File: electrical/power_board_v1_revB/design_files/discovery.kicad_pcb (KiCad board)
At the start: 2 copper layers, 150 x 100 mm, 18 parts, among them J1 Conn_02x04_CPU, J2 Conn_02x04_PCIe, J3 Conn_02x04_CPU, J4 Conn_02x04_PCIe, J5 Conn_02x04_PCIe, J6 Conn_02x04_PCIe

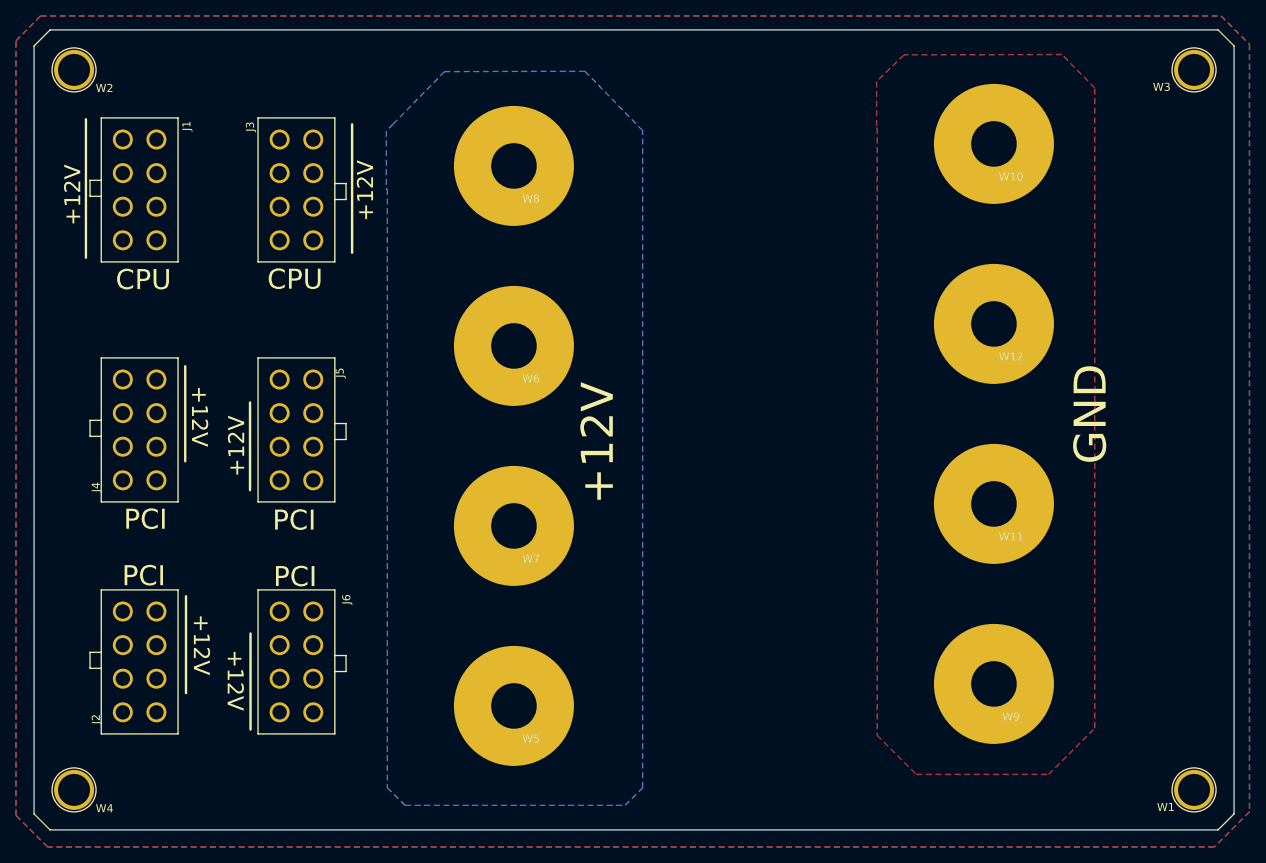
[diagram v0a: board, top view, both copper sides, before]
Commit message: Improvement
PCI connectors on the board have been modified into 2x3pins (2x4 pins originally).
Design and production files have been updated
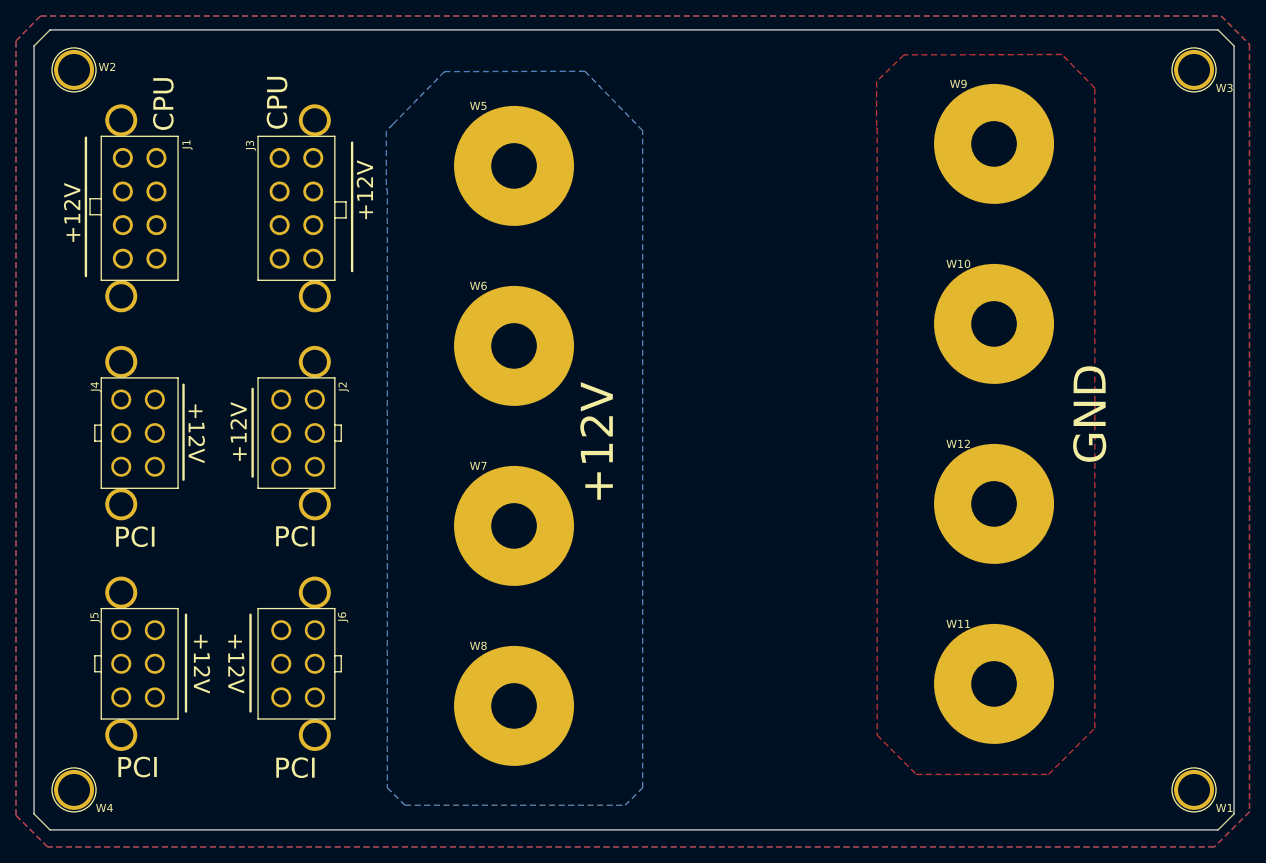
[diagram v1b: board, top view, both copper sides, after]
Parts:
- J1, J3: footprint footprint_cts:CONN_02x04_4.2mm -> discovery:CONN_02x04_4.2mm
- J2, J4, J5, J6: value Conn_02x04_PCIe -> Conn_02x03_PCIe; footprint footprint_cts:CONN_02x04_4.2mm -> discovery:CONN_02x03_4.2mm
- W1, W2, W3, W4: footprint TestPoint:TestPoint_Plated_Hole_D4.0mm -> discovery:FixingPoint_Plated_Hole_D4.0mm
- W10, W11, W12, W5, W6, W7, W8, W9: footprint footprint_cts:fixing_hole -> discovery:fixing_hole
- moved W5 67.5 mm to (60.0, 67.0), turned to 0 degrees
- moved W8 67.5 mm to (60.0, 134.5), turned to 0 degrees
- moved W9 67.5 mm to (120.0, 64.2), turned to 0 degrees
- moved J5 46.2 mm to (18.0, 136.1), turned to 90 degrees
- moved J2 45.6 mm to (28.0, 93.5), turned to 270 degrees
- moved W10 22.5 mm to (120.0, 86.8), turned to 0 degrees
- moved W11 22.5 mm to (120.0, 131.8), turned to 0 degrees
- moved W12 22.5 mm to (120.0, 109.2), turned to 0 degrees
- moved J6 2.33 mm to (28.0, 122.3)
- moved J1 2.30 mm to (18.0, 81.3)
- moved J3 2.30 mm to (28.0, 63.3)
- moved J4 1.70 mm to (18.0, 107.3)
- turned W6 to 0 degrees
- turned W7 to 0 degrees
